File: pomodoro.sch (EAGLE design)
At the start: 11 parts, among them IC1 ATTINY13-20PU, SW1 1825910-6

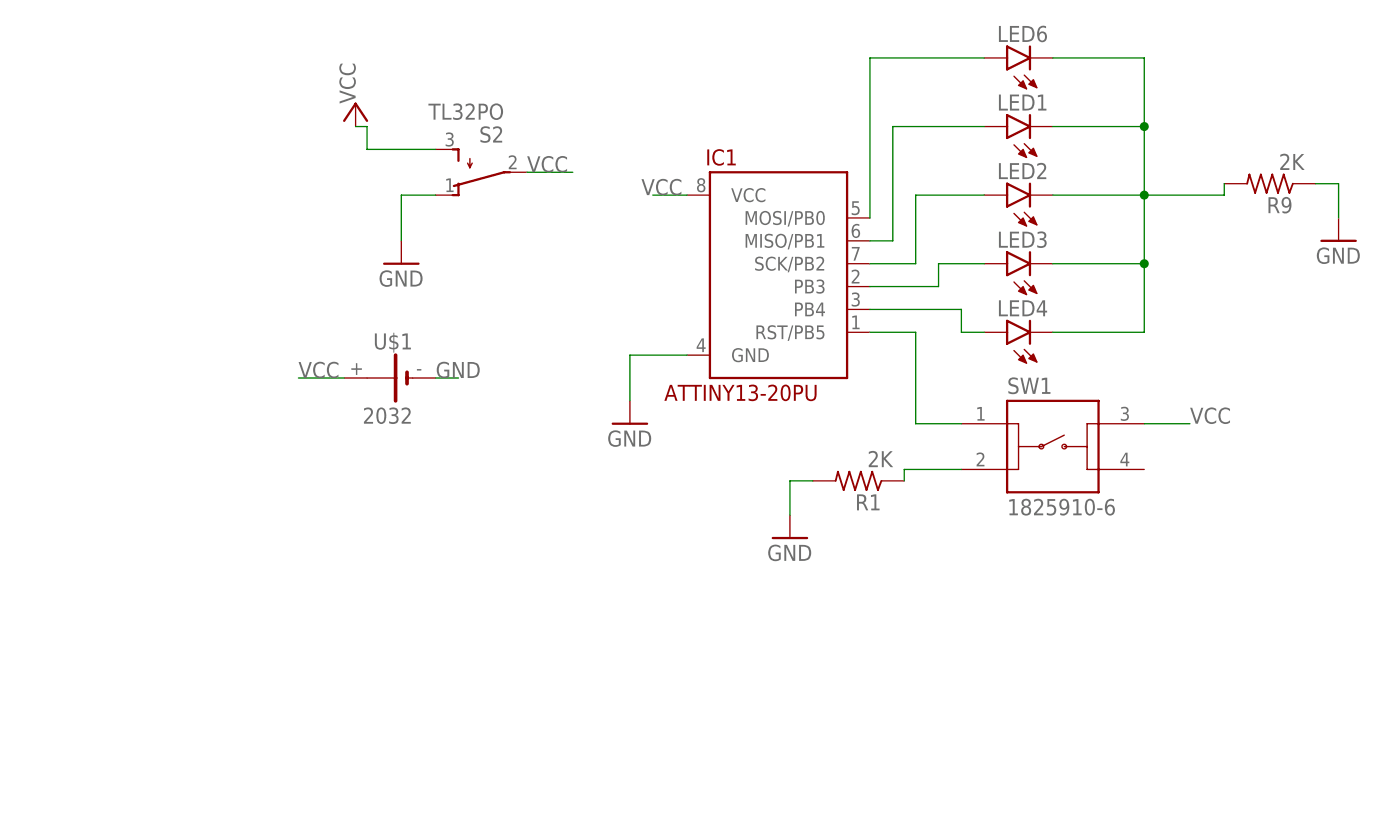
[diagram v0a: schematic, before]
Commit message: the circuit was redrawn
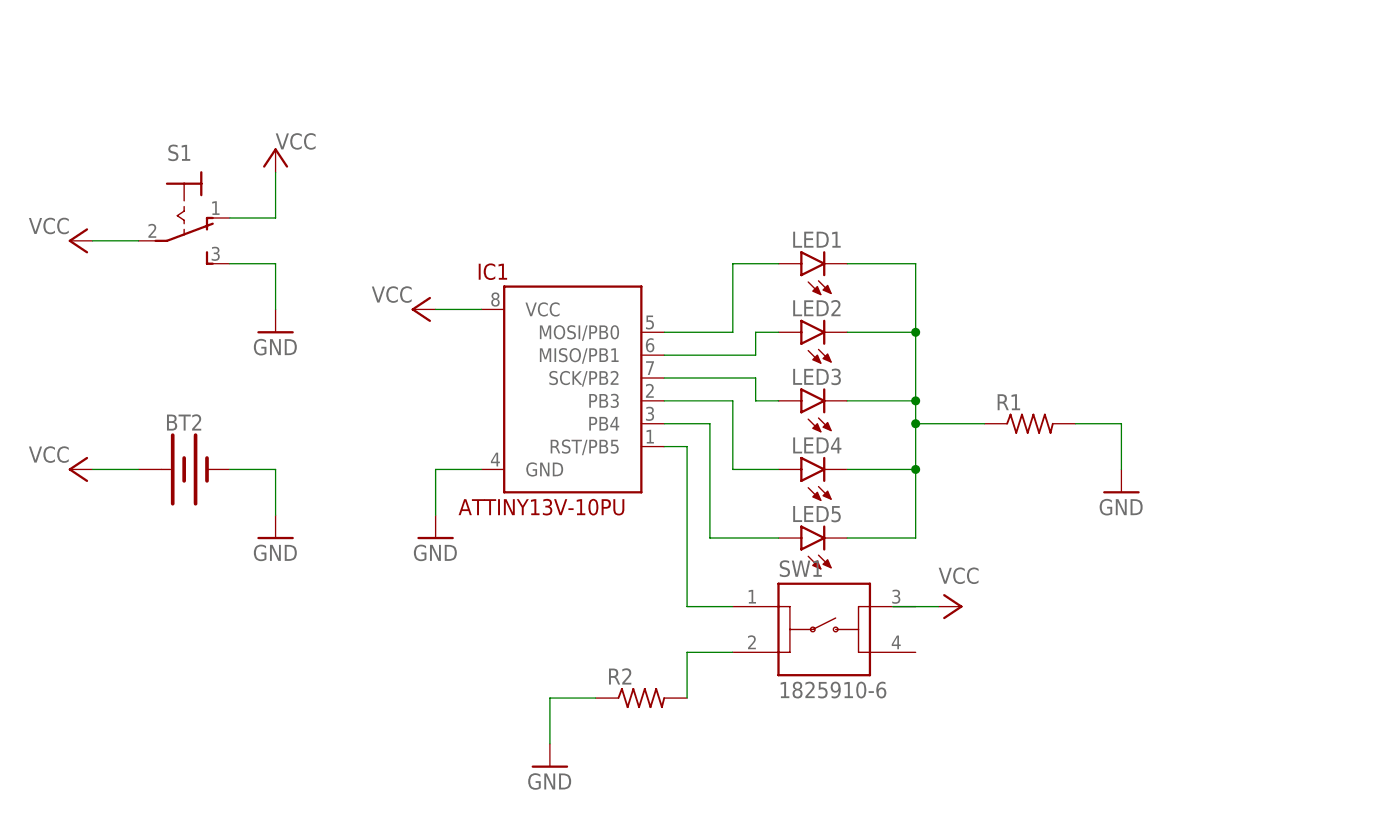
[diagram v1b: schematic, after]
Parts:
- removed LED6: (no value), led:LED3MM
- removed R9: 2K, rcl:R-US_0204/7
- removed S2: TL32PO, switch:TL32PO
- removed U$1: 2032, kzh20_lithium_batterie_holder:2032
- added BT2: (no value), SparkFun-Batteries:BATTERY-20MM_PTH_KIT
- added LED5: (no value), led:LED3MM
- added R2: (no value), adafruit:R-US_0207/9
- added S1: (no value), switch:320-916
- IC1: value ATTINY13-20PU -> ATTINY13V-10PU; device attiny13:ATTINY13-20PU -> attiny13:ATTINY13V-10PU
- R1: value 2K -> (none); device rcl:R-US_0204/7 -> adafruit:R-US_0207/9
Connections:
- net GND: now also BT2.-, R2.1, S1.S; no longer R9.1, S2.O, U$1.-
- net N$1: now also LED1.A; no longer LED6.A
- net N$2: now also LED2.A; no longer LED1.A
- net N$3: now also LED3.A; no longer LED2.A
- net N$4: now also LED4.A; no longer LED3.A
- net N$5: now also LED5.A; no longer LED4.A
- net N$6: now also LED5.C, R1.1; no longer LED6.C, R9.2
- net N$8: now also R2.2; no longer R1.1
- net VCC: now also BT2.+, S1.O, S1.P; no longer S2.P, S2.S, U$1.+
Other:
- moved on the sheet: IC1, LED1, LED2, LED3, LED4, R1, SW1

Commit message: curcuit changed
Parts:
- removed S1: (no value), switch:320-916
- R1, R2: device adafruit:R-US_0207/9 -> rcl:R-US_0204/7
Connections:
- net GND: now also R1.1, R2.2; no longer R1.2, R2.1, S1.S
- net N$6: now also R1.2; no longer R1.1
- net N$8: now also R2.1; no longer R2.2
- net VCC: no longer S1.O, S1.P
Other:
- moved on the sheet: R1, R2
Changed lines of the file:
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@@
 <setting verticaltext="up"/>
 </settings>
-<grid distance="0.1" unitdist="inch" unit="inch" style="lines" multiple="1" display="yes" altdistance="0.01" altunitdist="inch" altunit="inch"/>
+<grid distance="0.1" unitdist="inch" unit="inch" style="lines" multiple="1" display="no" altdistance="0.01" altunitdist="inch" altunit="inch"/>
 <layers>
 <layer number="1" name="Top" color="4" fill="1" visible="no" active="no"/>
@@
 </classes>
 <parts>
-<part name="P+1" library="supply1" library_urn="urn:adsk.eagle:library:371" deviceset="VCC" device=""/>
-<part name="S1" library="switch" library_urn="urn:adsk.eagle:library:380" deviceset="320-916" device="" package3d_urn="urn:adsk.eagle:package:27678/1" override_package3d_urn="urn:adsk.eagle:package:22087919/2" override_package_urn="urn:adsk.eagle:footprint:27534/1"/>
-<part name="GND1" library="supply1" library_urn="urn:adsk.eagle:library:371" deviceset="GND" device=""/>
-<part name="P+2" library="supply1" library_urn="urn:adsk.eagle:library:371" deviceset="VCC" device=""/>
 <part name="P+3" library="supply1" library_urn="urn:adsk.eagle:library:371" deviceset="VCC" device=""/>
 <part name="P+4" library="supply1" library_urn="urn:adsk.eagle:library:371" deviceset="VCC" device=""/>
@@
 <attribute name="PROD_ID" value="9031"/>
 </part>
-<part name="R1" library="adafruit" deviceset="R-US_" device="0207/9" package3d_urn="urn:adsk.eagle:package:6240935/1" override_package3d_urn="urn:adsk.eagle:package:22091099/2" override_package_urn="urn:adsk.eagle:footprint:6240292/1"/>
-<part name="R2" library="adafruit" deviceset="R-US_" device="0207/9" package3d_urn="urn:adsk.eagle:package:6240935/1" override_package3d_urn="urn:adsk.eagle:package:22091093/2" override_package_urn="urn:adsk.eagle:footprint:6240292/1"/>
 <part name="SW1" library="Switch" library_urn="urn:adsk.eagle:library:11396471" deviceset="1825910-6" device="" package3d_urn="urn:adsk.eagle:package:12788209/4"/>
+<part name="R1" library="rcl" library_urn="urn:adsk.eagle:library:334" deviceset="R-US_" device="0204/7" package3d_urn="urn:adsk.eagle:package:23498/2"/>
+<part name="R2" library="rcl" library_urn="urn:adsk.eagle:library:334" deviceset="R-US_" device="0204/7" package3d_urn="urn:adsk.eagle:package:23498/2"/>
 </parts>
 <sheets>
@@
 </plain>
 <instances>
-<instance part="P+1" gate="VCC" x="-7.62" y="71.12" smashed="yes">
-<attribute name="VALUE" x="-7.62" y="71.12" size="1.778" layer="96"/>
-</instance>
-<instance part="S1" gate="1" x="-17.78" y="63.5" smashed="yes" rot="R270">
-<attribute name="NAME" x="-19.685" y="69.85" size="1.778" layer="95"/>
-<attribute name="VALUE" x="-15.24" y="67.31" size="1.778" layer="96"/>
-</instance>
-<instance part="GND1" gate="1" x="-7.62" y="50.8" smashed="yes">
-<attribute name="VALUE" x="-10.16" y="48.26" size="1.778" layer="96"/>
-</instance>
-<instance part="P+2" gate="VCC" x="-30.48" y="60.96" smashed="yes" rot="R90">
-<attribute name="VALUE" x="-30.48" y="63.5" size="1.778" layer="96" rot="R180"/>
-</instance>
 <instance part="P+3" gate="VCC" x="68.58" y="20.32" smashed="yes" rot="R270">
 <attribute name="VALUE" x="66.04" y="22.86" size="1.778" layer="96"/>
@@
 <attribute name="VALUE" x="-17.78" y="31.242" size="1.778" layer="96" font="vector" align="top-center"/>
 </instance>
-<instance part="R1" gate="G$1" x="76.2" y="40.64" smashed="yes">
-<attribute name="NAME" x="72.39" y="42.1386" size="1.778" layer="95"/>
-<attribute name="VALUE" x="72.39" y="37.338" size="1.778" layer="96"/>
-</instance>
-<instance part="R2" gate="G$1" x="33.02" y="10.16" smashed="yes">
-<attribute name="NAME" x="29.21" y="11.6586" size="1.778" layer="95"/>
-<attribute name="VALUE" x="29.21" y="6.858" size="1.778" layer="96"/>
-</instance>
 <instance part="SW1" gate="G$1" x="53.34" y="17.78" smashed="yes">
 <attribute name="NAME" x="48.2503" y="23.63315" size="1.803440625" layer="95"/>
 <attribute name="VALUE" x="48.251690625" y="10.14753125" size="1.802940625" layer="96"/>
+</instance>
+<instance part="R1" gate="G$1" x="76.2" y="40.64" smashed="yes" rot="R180">
+<attribute name="NAME" x="78.74" y="39.1414" size="1.778" layer="95" rot="R180"/>
+<attribute name="VALUE" x="80.01" y="43.942" size="1.778" layer="96" rot="R180"/>
+</instance>
+<instance part="R2" gate="G$1" x="33.02" y="10.16" smashed="yes" rot="R180">
+<attribute name="NAME" x="35.56" y="8.6614" size="1.778" layer="95" rot="R180"/>
+<attribute name="VALUE" x="36.83" y="13.462" size="1.778" layer="96" rot="R180"/>
 </instance>
 </instances>
@@
 <net name="VCC" class="0">
 <segment>
-<pinref part="P+2" gate="VCC" pin="VCC"/>
-<pinref part="S1" gate="1" pin="P"/>
-<wire x1="-27.94" y1="60.96" x2="-22.86" y2="60.96" width="0.1524" layer="91"/>
-</segment>
-<segment>
-<pinref part="S1" gate="1" pin="O"/>
-<wire x1="-12.7" y1="63.5" x2="-7.62" y2="63.5" width="0.1524" layer="91"/>
-<pinref part="P+1" gate="VCC" pin="VCC"/>
-<wire x1="-7.62" y1="63.5" x2="-7.62" y2="68.58" width="0.1524" layer="91"/>
-</segment>
-<segment>
 <pinref part="P+4" gate="VCC" pin="VCC"/>
 <wire x1="-27.94" y1="35.56" x2="-22.86" y2="35.56" width="0.1524" layer="91"/>
@@
 <net name="GND" class="0">
 <segment>
-<pinref part="S1" gate="1" pin="S"/>
-<wire x1="-12.7" y1="58.42" x2="-7.62" y2="58.42" width="0.1524" layer="91"/>
-<pinref part="GND1" gate="1" pin="GND"/>
-<wire x1="-7.62" y1="58.42" x2="-7.62" y2="53.34" width="0.1524" layer="91"/>
-</segment>
-<segment>
 <wire x1="-12.7" y1="35.56" x2="-7.62" y2="35.56" width="0.1524" layer="91"/>
 <pinref part="GND2" gate="1" pin="GND"/>
@@
 <pinref part="GND4" gate="1" pin="GND"/>
 <wire x1="86.36" y1="40.64" x2="86.36" y2="35.56" width="0.1524" layer="91"/>
-<pinref part="R1" gate="G$1" pin="2"/>
+<pinref part="R1" gate="G$1" pin="1"/>
 </segment>
 <segment>
@@
 <pinref part="GND5" gate="1" pin="GND"/>
 <wire x1="22.86" y1="10.16" x2="22.86" y2="5.08" width="0.1524" layer="91"/>
-<pinref part="R2" gate="G$1" pin="1"/>
+<pinref part="R2" gate="G$1" pin="2"/>
 </segment>
 </net>
@@
 <wire x1="63.5" y1="40.64" x2="71.12" y2="40.64" width="0.1524" layer="91"/>
 <junction x="63.5" y="40.64"/>
-<pinref part="R1" gate="G$1" pin="1"/>
+<pinref part="R1" gate="G$1" pin="2"/>
 </segment>
 </net>
@@
 <wire x1="38.1" y1="10.16" x2="38.1" y2="15.24" width="0.1524" layer="91"/>
 <wire x1="38.1" y1="15.24" x2="43.18" y2="15.24" width="0.1524" layer="91"/>
-<pinref part="R2" gate="G$1" pin="2"/>
 <pinref part="SW1" gate="G$1" pin="2"/>
-</segment>
-</net>
+<pinref part="R2" gate="G$1" pin="1"/>
+</segment>
+</net>
